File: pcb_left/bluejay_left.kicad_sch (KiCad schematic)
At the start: 81 parts, among them J1 SJ-43514, U1 ATmega328P-PU, Y1 16MHz

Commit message: remove mounting hole 9
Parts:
- removed H9: M2, MountingHole:MountingHole_2.2mm_M2_Pad, symbol Mechanical:MountingHole
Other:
- note added: "Ground some mounting holes so as to ground main pcb to plate and base."
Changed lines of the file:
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@@
+    (effects (font (size 1.27 1.27)) (justify left bottom))
+  )
+  (text "Ground some mounting holes so as to ground \nmain pcb to plate and base."
+    (at 208.28 177.8 0)
     (effects (font (size 1.27 1.27)) (justify left bottom))
   )
@@
     )
     (pin "1")
-  )
-  (symbol (lib_id "Mechanical:MountingHole") (at 257.81 154.94 0) (unit 1)
-    (in_bom no) (on_board yes) (fields_autoplaced)
-    (property "Reference" "H9" (id 0) (at 260.35 153.6699 0)
-      (effects (font (size 1.27 1.27)) (justify left))
-    )
-    (property "Value" "M2" (id 1) (at 260.35 156.2099 0)
-      (effects (font (size 1.27 1.27)) (justify left))
-    )
-    (property "Footprint" "MountingHole:MountingHole_2.2mm_M2_Pad" (id 2) (at 257.81 154.94 0)
-      (effects (font (size 1.27 1.27)) hide)
-    )
-    (property "Datasheet" "~" (id 3) (at 257.81 154.94 0)
-      (effects (font (size 1.27 1.27)) hide)
-    )
   )
   (symbol (lib_id "Diode_AKL:1N4148") (at 162.56 99.06 180) (unit 1)
@@
       (reference "H8") (unit 1) (value "M2") (footprint "MountingHole:MountingHole_2.2mm_M2_Pad")
     )
-    (path "/88babb1f-a86c-44c4-9ecd-f3e8d1f4aef4"
-      (reference "H9") (unit 1) (value "M2") (footprint "MountingHole:MountingHole_2.2mm_M2_Pad")
-    )
     (path "/36a90cbb-ec70-4202-aacd-9cf629bac560"

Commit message: Update placement of some components and size of drill holes
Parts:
- removed H7, H8: M2, MountingHole:MountingHole_2.2mm_M2_Pad, symbol Mechanical:MountingHole
- H2: symbol Mechanical:MountingHole_Pad -> Mechanical:MountingHole
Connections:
- net GND: no longer H2.1
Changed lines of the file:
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@@
   (junction (at 182.88 111.76) (diameter 0) (color 0 0 0 0)
-  )
-  (junction (at 215.9 167.64) (diameter 0) (color 0 0 0 0)
   )
   (junction (at 207.01 111.76) (diameter 0) (color 0 0 0 0)
@@
     (stroke (width 0) (type default) (color 0 0 0 0))
   )
-  (wire (pts (xy 208.28 167.64) (xy 215.9 167.64))
-    (stroke (width 0) (type default) (color 0 0 0 0))
-  )
   (wire (pts (xy 50.8 102.87) (xy 50.8 104.14))
     (stroke (width 0) (type default) (color 0 0 0 0))
@@
   )
   (wire (pts (xy 115.57 162.56) (xy 116.84 162.56))
-    (stroke (width 0) (type default) (color 0 0 0 0))
-  )
-  (wire (pts (xy 215.9 165.1) (xy 215.9 167.64))
     (stroke (width 0) (type default) (color 0 0 0 0))
   )
@@
     (pin "2")
   )
-  (symbol (lib_id "Mechanical:MountingHole_Pad") (at 215.9 162.56 0) (unit 1)
+  (symbol (lib_name "MountingHole_1") (lib_id "Mechanical:MountingHole") (at 215.9 162.56 0) (unit 1)
     (in_bom yes) (on_board yes) (fields_autoplaced)
     (property "Reference" "H2" (id 0) (at 218.44 161.2899 0)
@@
       (effects (font (size 1.27 1.27)) hide)
     )
-    (pin "1")
   )
   (symbol (lib_id "power:GND") (at 50.8 111.76 0) (unit 1)
@@
     (pin "1")
     (pin "2")
-  )
-  (symbol (lib_id "Mechanical:MountingHole") (at 247.65 154.94 0) (unit 1)
-    (in_bom no) (on_board yes) (fields_autoplaced)
-    (property "Reference" "H7" (id 0) (at 250.19 153.6699 0)
-      (effects (font (size 1.27 1.27)) (justify left))
-    )
-    (property "Value" "M2" (id 1) (at 250.19 156.2099 0)
-      (effects (font (size 1.27 1.27)) (justify left))
-    )
-    (property "Footprint" "MountingHole:MountingHole_2.2mm_M2_Pad" (id 2) (at 247.65 154.94 0)
-      (effects (font (size 1.27 1.27)) hide)
-    )
-    (property "Datasheet" "~" (id 3) (at 247.65 154.94 0)
-      (effects (font (size 1.27 1.27)) hide)
-    )
   )
   (symbol (lib_id "Diode_AKL:1N4148") (at 138.43 99.06 180) (unit 1)
@@
     (pin "2")
   )
-  (symbol (lib_id "Mechanical:MountingHole") (at 247.65 162.56 0) (unit 1)
-    (in_bom no) (on_board yes) (fields_autoplaced)
-    (property "Reference" "H8" (id 0) (at 250.19 161.2899 0)
-      (effects (font (size 1.27 1.27)) (justify left))
-    )
-    (property "Value" "M2" (id 1) (at 250.19 163.8299 0)
-      (effects (font (size 1.27 1.27)) (justify left))
-    )
-    (property "Footprint" "MountingHole:MountingHole_2.2mm_M2_Pad" (id 2) (at 247.65 162.56 0)
-      (effects (font (size 1.27 1.27)) hide)
-    )
-    (property "Datasheet" "~" (id 3) (at 247.65 162.56 0)
-      (effects (font (size 1.27 1.27)) hide)
-    )
-  )
   (symbol (lib_id "BlueJaySymbolLibrary:Switch_SW_Push") (at 194.31 81.28 90) (unit 1)
     (in_bom yes) (on_board yes) (fields_autoplaced)
@@
     (pin "2")
   )
-  (symbol (lib_id "power:GND") (at 215.9 167.64 0) (unit 1)
-    (in_bom yes) (on_board yes) (fields_autoplaced)
-    (property "Reference" "#PWR0115" (id 0) (at 215.9 173.99 0)
-      (effects (font (size 1.27 1.27)) hide)
-    )
-    (property "Value" "GND" (id 1) (at 215.9 171.45 0)
-      (effects (font (size 1.27 1.27)) hide)
-    )
-    (property "Footprint" "" (id 2) (at 215.9 167.64 0)
-      (effects (font (size 1.27 1.27)) hide)
-    )
-    (property "Datasheet" "~" (id 3) (at 215.9 167.64 0)
+  (symbol (lib_id "power:GND") (at 208.28 167.64 0) (unit 1)
+    (in_bom yes) (on_board yes) (fields_autoplaced)
+    (property "Reference" "#PWR0115" (id 0) (at 208.28 173.99 0)
+      (effects (font (size 1.27 1.27)) hide)
+    )
+    (property "Value" "GND" (id 1) (at 208.28 171.45 0)
+      (effects (font (size 1.27 1.27)) hide)
+    )
+    (property "Footprint" "" (id 2) (at 208.28 167.64 0)
+      (effects (font (size 1.27 1.27)) hide)
+    )
+    (property "Datasheet" "~" (id 3) (at 208.28 167.64 0)
       (effects (font (size 1.27 1.27)) hide)
     )
@@
       (reference "H6") (unit 1) (value "M2") (footprint "MountingHole:MountingHole_2.2mm_M2_Pad")
     )
-    (path "/8ff55002-cb98-4e23-b57e-209cc7ec712a"
-      (reference "H7") (unit 1) (value "M2") (footprint "MountingHole:MountingHole_2.2mm_M2_Pad")
-    )
-    (path "/a73aae4f-b04b-4d16-8b11-ca3d57da8772"
-      (reference "H8") (unit 1) (value "M2") (footprint "MountingHole:MountingHole_2.2mm_M2_Pad")
-    )
     (path "/36a90cbb-ec70-4202-aacd-9cf629bac560"

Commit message: Update gerber files
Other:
- note added: "Ground some mounting holes so as to ground main pcb to base."
- note removed: "Ground some mounting holes so as to ground main pcb to plate and base."
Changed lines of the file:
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@@
     (effects (font (size 1.27 1.27)) (justify left bottom))
   )
-  (text "Ground some mounting holes so as to ground \nmain pcb to plate and base."
+  (text "Ground some mounting holes so as to ground \nmain pcb to base."
     (at 208.28 177.8 0)
     (effects (font (size 1.27 1.27)) (justify left bottom))

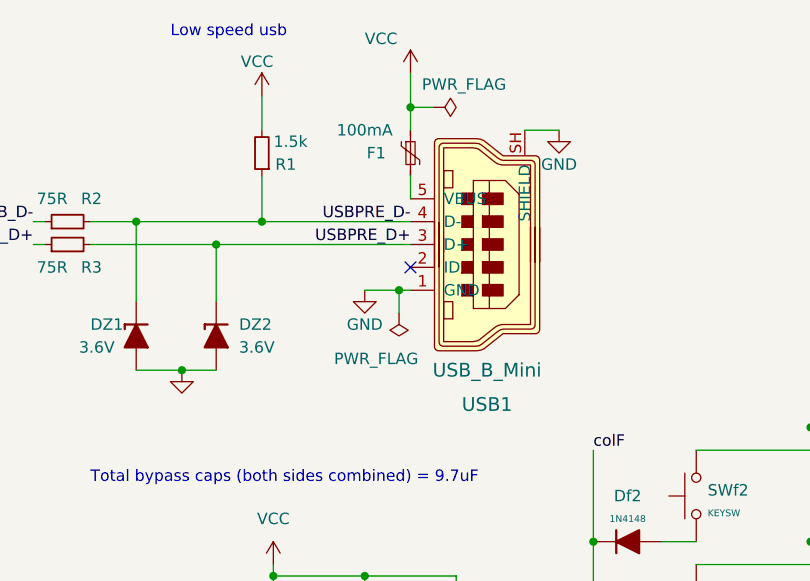
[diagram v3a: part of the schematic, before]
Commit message: fix routing with usb connector
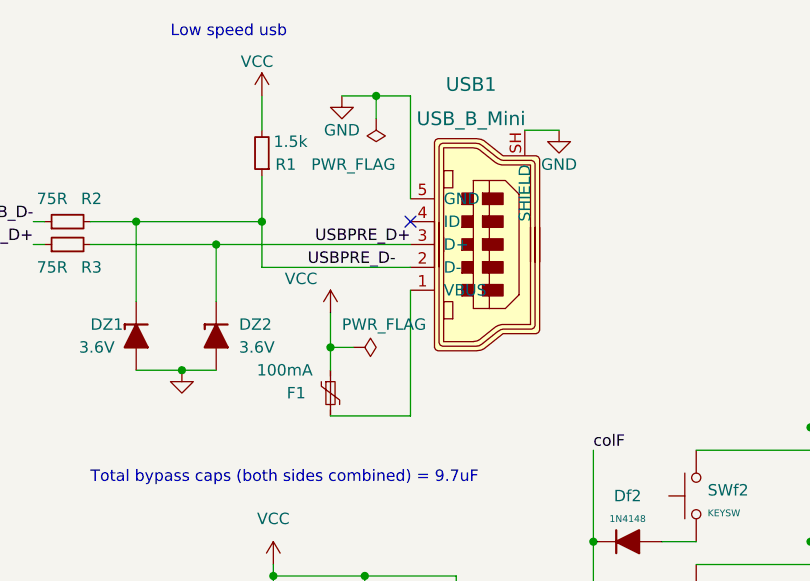
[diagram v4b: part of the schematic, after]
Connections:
- net GND: now also USB1.5 (GND); no longer USB1.1 (GND)
- net USBPRE_D-: now also USB1.2 (D-); no longer USB1.4 (D-)
- net at F1.2: now also USB1.1 (VBUS); no longer USB1.5 (VBUS)
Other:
- moved on the sheet: F1
